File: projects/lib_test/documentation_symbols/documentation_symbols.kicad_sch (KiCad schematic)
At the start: 1 part

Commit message: updated test projects
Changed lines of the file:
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@@
 (kicad_sch
-	(version 20231120)
+	(version 20250114)
 	(generator "eeschema")
-	(generator_version "8.0")
+	(generator_version "9.0")
 	(paper "A4")
 	(title_block
 		(title "Documentation symbols")
-		(date "2025-02-08")
+		(date "2025-05-24")
 		(rev "1")
 		(comment 1 "-")
@@
 		)
 	)
+	(embedded_fonts no)
 )

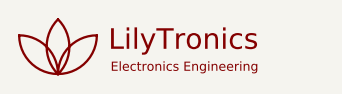
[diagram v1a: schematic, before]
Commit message: updated documentation test design
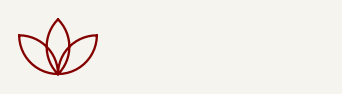
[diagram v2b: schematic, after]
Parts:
- removed DOC1001: logo_lilytronics, lily_footprints:logo_lilytronics, symbol lily_symbols:logo_lilytronics
- added DOC1001: doc_logo_lilytronics, lily_footprints:doc_logo_lilytronics, symbol lily_symbols:doc_logo_lilytronics
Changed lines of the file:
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@@
 	)
 	(symbol
-		(lib_id "lily_symbols:logo_lilytronics")
+		(lib_id "lily_symbols:doc_logo_lilytronics")
 		(at 25.4 25.4 0)
 		(unit 1)
@@
 			)
 		)
-		(property "Value" "logo_lilytronics"
+		(property "Value" "doc_logo_lilytronics"
 			(at 25.4 27.94 0)
 			(effects
@@
 			)
 		)
-		(property "Footprint" "lily_footprints:logo_lilytronics"
+		(property "Footprint" "lily_footprints:doc_logo_lilytronics"
 			(at 25.4 35.56 0)
 			(effects
